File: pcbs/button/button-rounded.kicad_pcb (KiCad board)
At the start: 2 copper layers, 64.1 x 68.9 mm, 20 parts, among them J1 Conn_01x08, SW1 CAP-BUTTON, U1 CAP1293

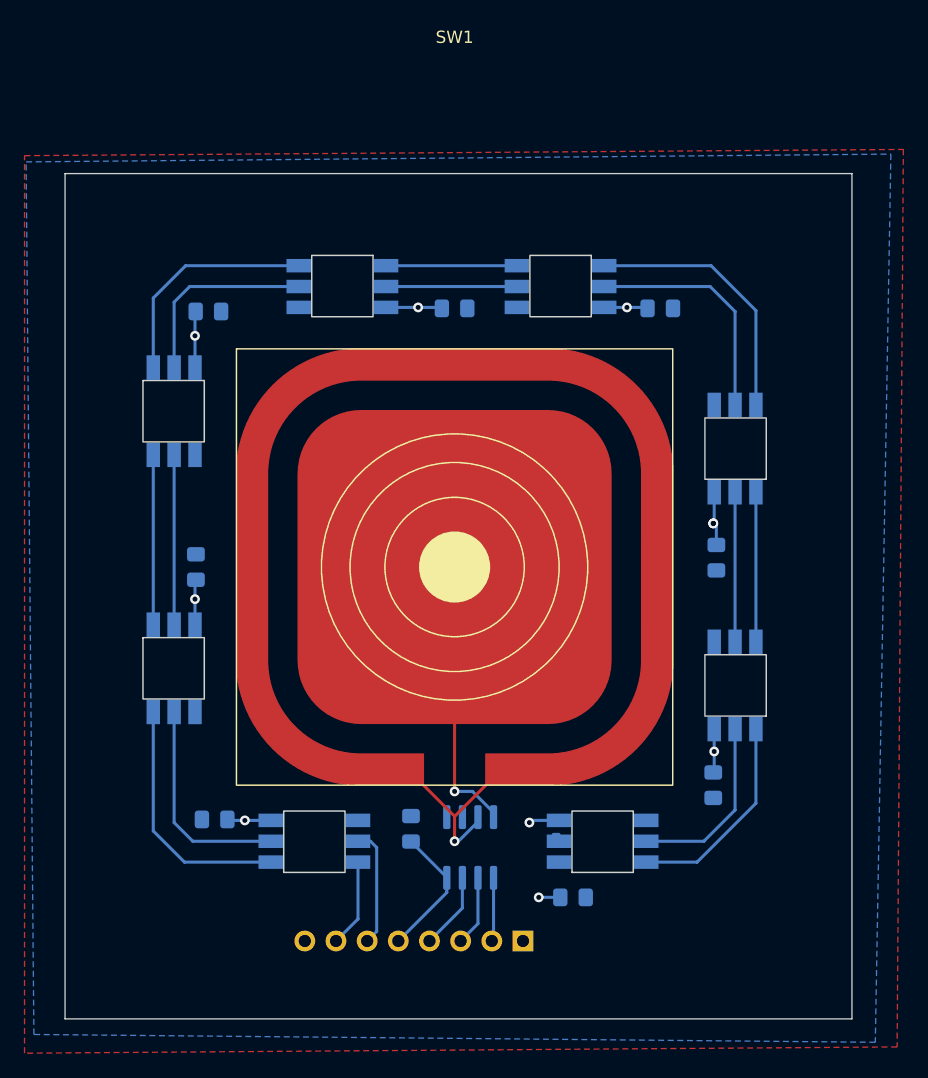
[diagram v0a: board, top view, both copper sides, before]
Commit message: Add PCB for capacitive button
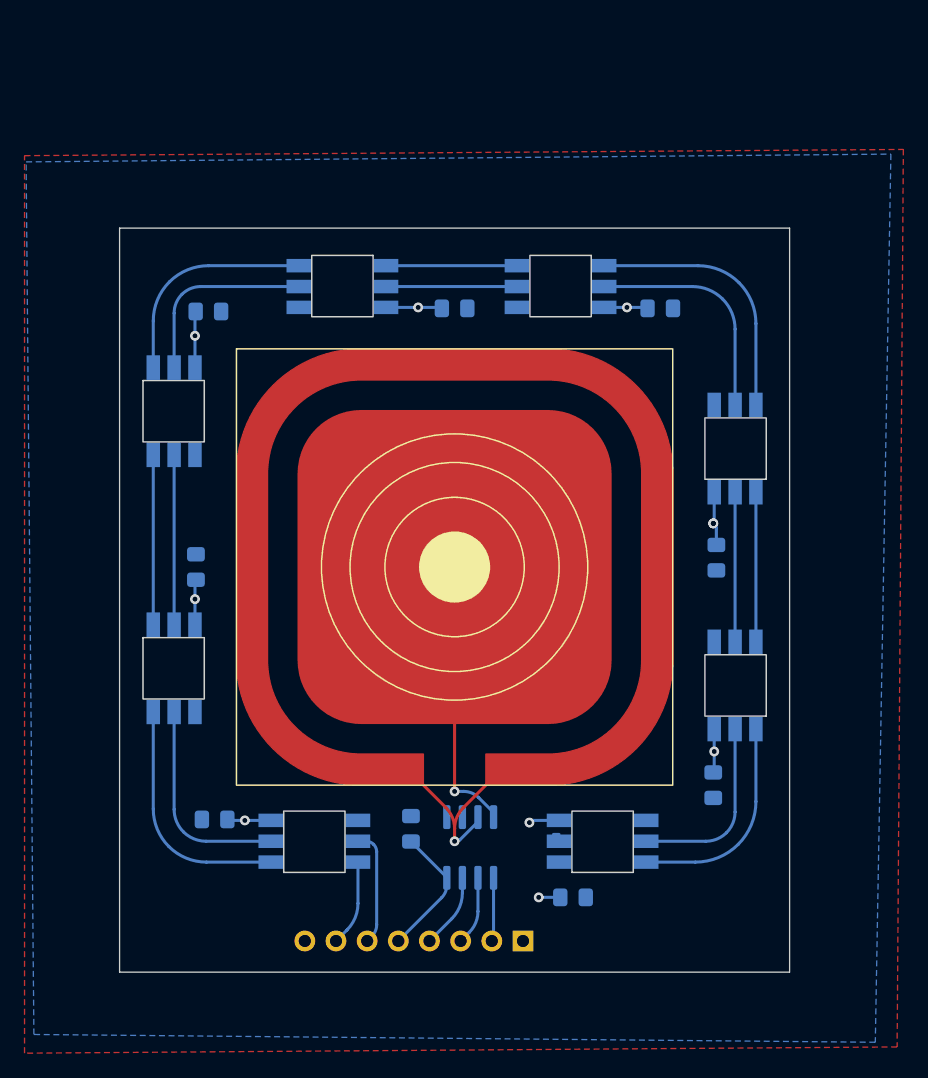
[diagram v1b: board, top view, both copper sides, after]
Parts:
- renumbered D1 to De, D2 to De, D8 to De, D3 to De
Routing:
- net Net-(SW1-Pad2): track 15.7 -> 16.4 mm
- net Net-(D7-Pad6): track 17.0 -> 17.6 mm
- net Net-(SW1-Pad1): track 23.5 -> 22.9 mm
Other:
- board size 64.1 x 68.9 mm -> 54.6 x 60.6 mm

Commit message: Add teardrops to capacitive button PCB.
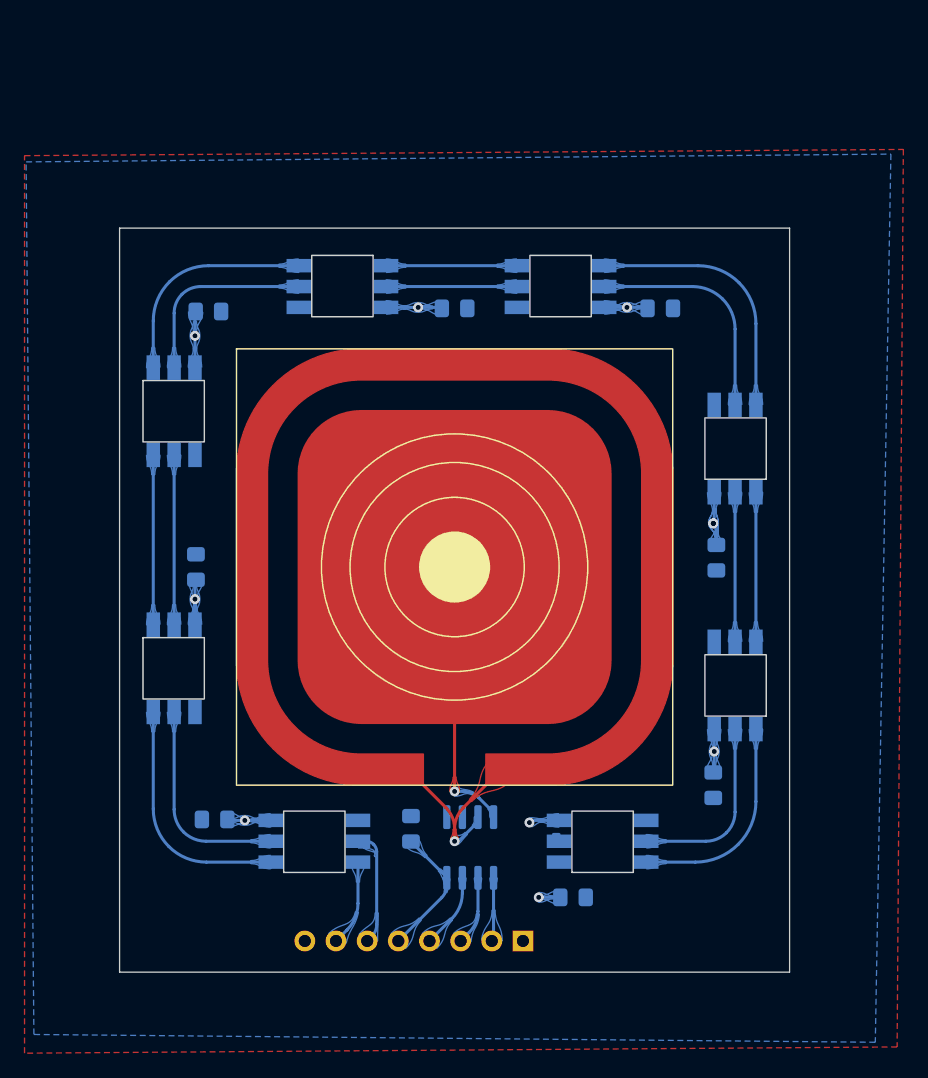
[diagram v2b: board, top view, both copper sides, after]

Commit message: remove outer border from touch pad silkscreen
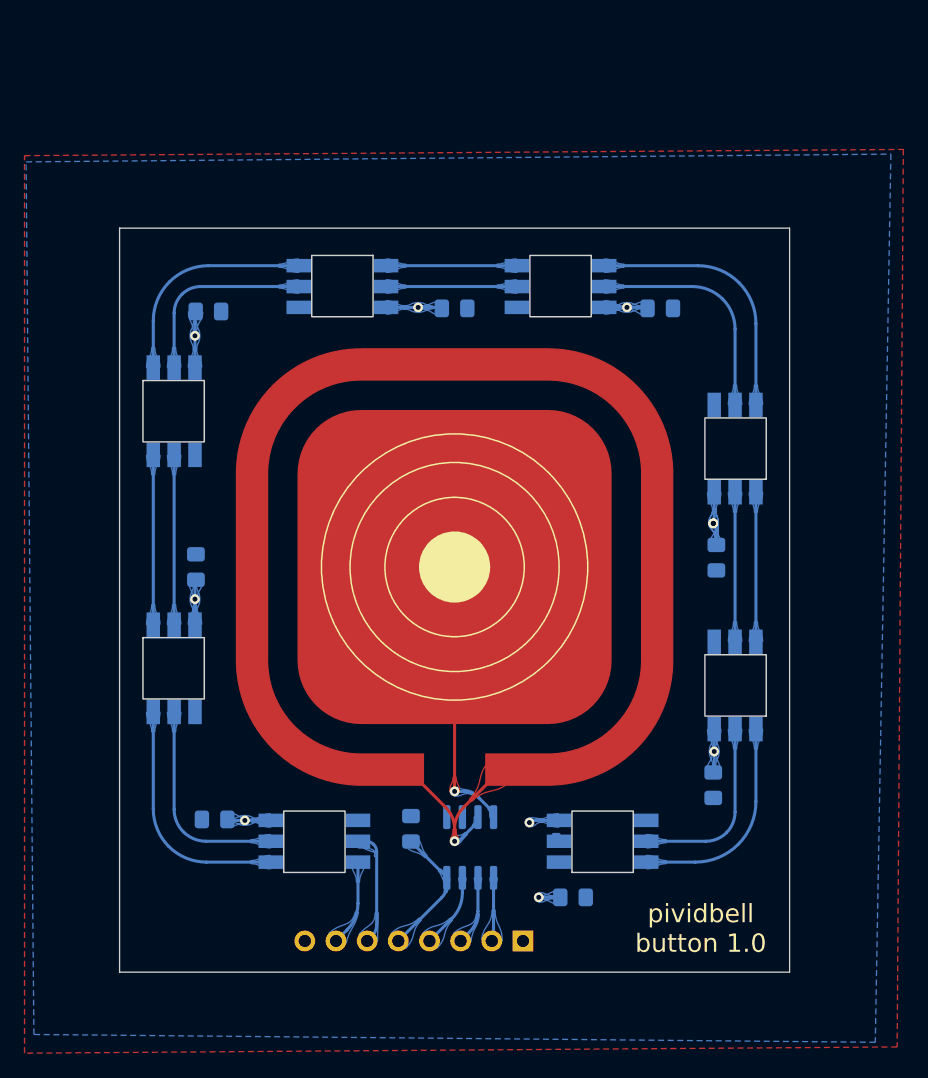
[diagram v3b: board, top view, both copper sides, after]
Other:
- board text added: "pividbell button 1.0"
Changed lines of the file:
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@@
       (effects (font (size 1 1) (thickness 0.15)))
     )
-    (fp_rect (start -17.78 -17.78) (end 17.78 17.78) (layer "F.SilkS") (width 0.12) (fill none))
+    (fp_circle (center 0 0) (end 2.839806 0) (layer "F.SilkS") (width 0.12) (fill solid))
+    (fp_circle (center 0 0) (end 10.16 -3.81) (layer "F.SilkS") (width 0.12) (fill none))
     (fp_circle (center 0 0) (end 5.08 -2.54) (layer "F.SilkS") (width 0.12) (fill none))
-    (fp_circle (center 0 0) (end 10.16 -3.81) (layer "F.SilkS") (width 0.12) (fill none))
     (fp_circle (center 0 0) (end 7.62 -3.81) (layer "F.SilkS") (width 0.12) (fill none))
-    (fp_circle (center 0 0) (end 2.839806 0) (layer "F.SilkS") (width 0.12) (fill solid))
     (pad "1" smd custom (at 0 0) (size 25 25) (layers "F.Cu" "F.Paste" "F.Mask")
       (net 25 "Net-(SW1-Pad1)") (pinfunction "INNER") (pintype "passive")
@@
   )
   (gr_rect (start 61.595 121.92) (end 116.205 61.2775) (layer "Edge.Cuts") (width 0.1) (fill none))
+  (gr_text "pividbell\nbutton 1.0" (at 108.966 118.364) (layer "F.SilkS")
+    (effects (font (size 1.5 1.5) (thickness 0.3)))
+  )
   (segment (start 88.265 114.25525) (end 88.265 114.8315) (width 0.25) (layer "B.Cu") (net 1))
   (segment (start 88.265 114.21475) (end 88.265 114.25525) (width 0.25) (layer "B.Cu") (net 1))
